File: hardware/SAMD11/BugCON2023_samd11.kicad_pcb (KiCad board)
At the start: 2 copper layers, 122.4 x 97.9 mm, 35 parts, among them J1 I2C, J3 PAD2, J4 PAD, P1 USB_C_Plug_USB2.0, Q1 DMG3415U-7, SW2 ON, U1 ATSAMD11C14A-SS, U2 AP2112K-3.3

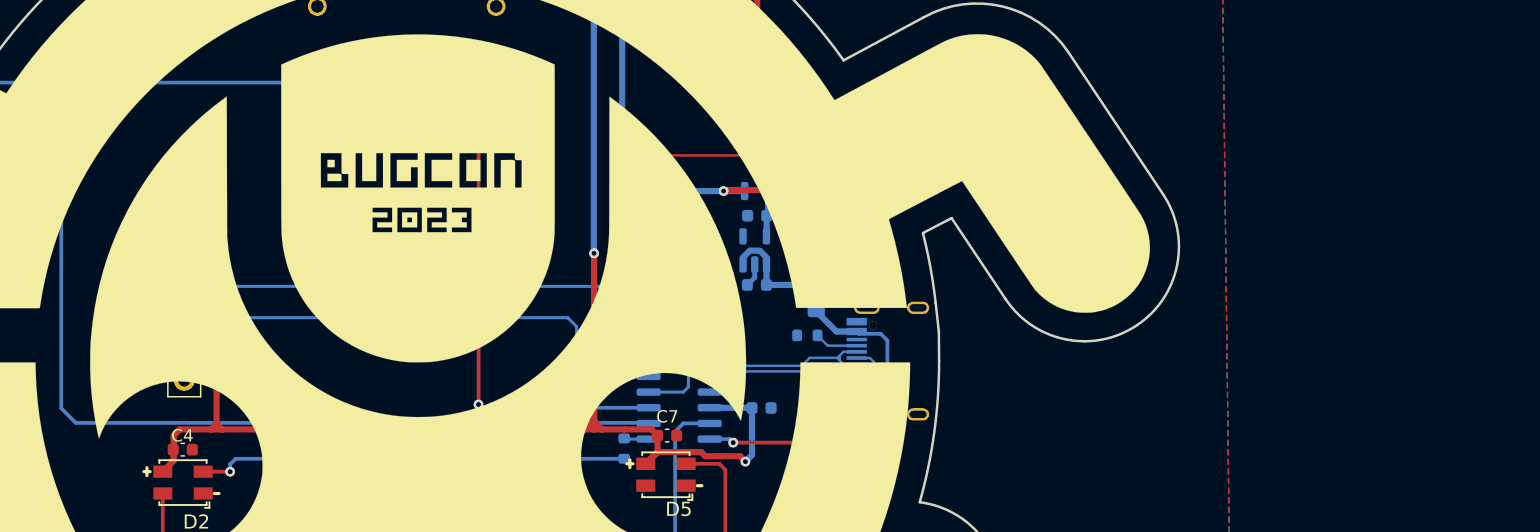
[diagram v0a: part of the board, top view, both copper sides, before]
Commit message: change MCU for RP2040
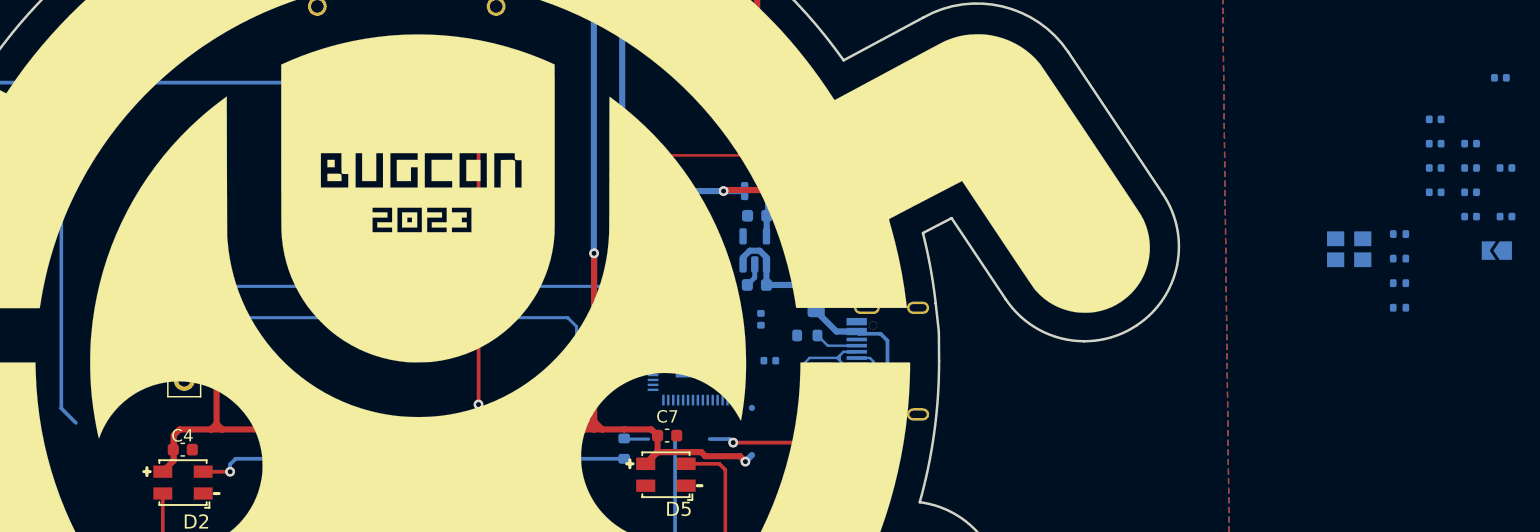
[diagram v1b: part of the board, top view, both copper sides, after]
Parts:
- removed U1: ATSAMD11C14A-SS, Package_SO:SOIC-14_3.9x8.7mm_P1.27mm
- added C10: 0.1uF, Capacitor_SMD:C_0402_1005Metric, B.Cu at (167.7, 101.7)
- added C11: 27pF, Capacitor_SMD:C_0402_1005Metric, B.Cu at (238.7, 90.3)
- added C12: 0.1uF, Capacitor_SMD:C_0402_1005Metric, B.Cu at (179.0, 102.0)
- added C13: 1uF, Capacitor_SMD:C_0402_1005Metric, B.Cu at (235.8, 84.4)
- added C14: 0.1uF, Capacitor_SMD:C_0402_1005Metric, B.Cu at (235.8, 86.4)
- added C15: 0.1uF, Capacitor_SMD:C_0402_1005Metric, B.Cu at (235.8, 88.3)
- added C16: 0.1uF, Capacitor_SMD:C_0402_1005Metric, B.Cu at (235.8, 90.3)
- added C17: 0.1uF, Capacitor_SMD:C_0402_1005Metric, B.Cu at (233.0, 82.4)
- added C18: 0.1uF, Capacitor_SMD:C_0402_1005Metric, B.Cu at (233.0, 84.4)
- added C19: 0.1uF, Capacitor_SMD:C_0402_1005Metric, B.Cu at (233.0, 86.4)
- added C20: 0.1uF, Capacitor_SMD:C_0402_1005Metric, B.Cu at (233.0, 88.3)
- added C8: 1uF, Capacitor_SMD:C_0402_1005Metric, B.Cu at (178.3, 98.7)
- added C9: 27pF, Capacitor_SMD:C_0402_1005Metric, B.Cu at (238.7, 86.4)
- added JP1: BOOT, Jumper:SolderJumper-2_P1.3mm_Open_TrianglePad1.0x1.5mm, B.Cu at (238.0, 93.1)
- added R10: 10k, Resistor_SMD:R_0402_1005Metric, B.Cu at (230.1, 97.7)
- added R7: 27, Resistor_SMD:R_0402_1005Metric, B.Cu at (230.1, 91.7)
- added R8: 27, Resistor_SMD:R_0402_1005Metric, B.Cu at (230.1, 93.7)
- added R9: 1k, Resistor_SMD:R_0402_1005Metric, B.Cu at (230.1, 95.7)
- added U3: RP2040, Package_DFN_QFN:QFN-56-1EP_7x7mm_P0.4mm_EP3.2x3.2mm, B.Cu at (173.0, 101.8)
- added Y1: 12MHz, Crystal:Crystal_SMD_3225-4Pin_3.2x2.5mm, B.Cu at (226.0, 93.0)
- C1: value 100nF -> 0.1uF; footprint Capacitor_SMD:C_0603_1608Metric -> Capacitor_SMD:C_0402_1005Metric
- moved C1 65.6 mm to (238.3, 79.1), turned to 180 degrees
- renumbered JE to J5
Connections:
- J4 pad : /IN1 -> (no net)
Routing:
- net /TX: track 94.6 -> 48.1 mm
- net /RX: track 95.4 -> 81.8 mm
- net /SDA: track 55.4 -> 44.5 mm
- net /D+: track 16.0 -> 8.16 mm
- net /D-: track 14.8 -> 7.20 mm
- net +3.3V: track 172.5 -> 165.2 mm
- net /RST: track 63.7 -> 57.3 mm
- net /SCL: track 44.3 -> 40.0 mm
- net /IN2: track 94.0 -> 90.9 mm
- net GND: vias 3 -> 2

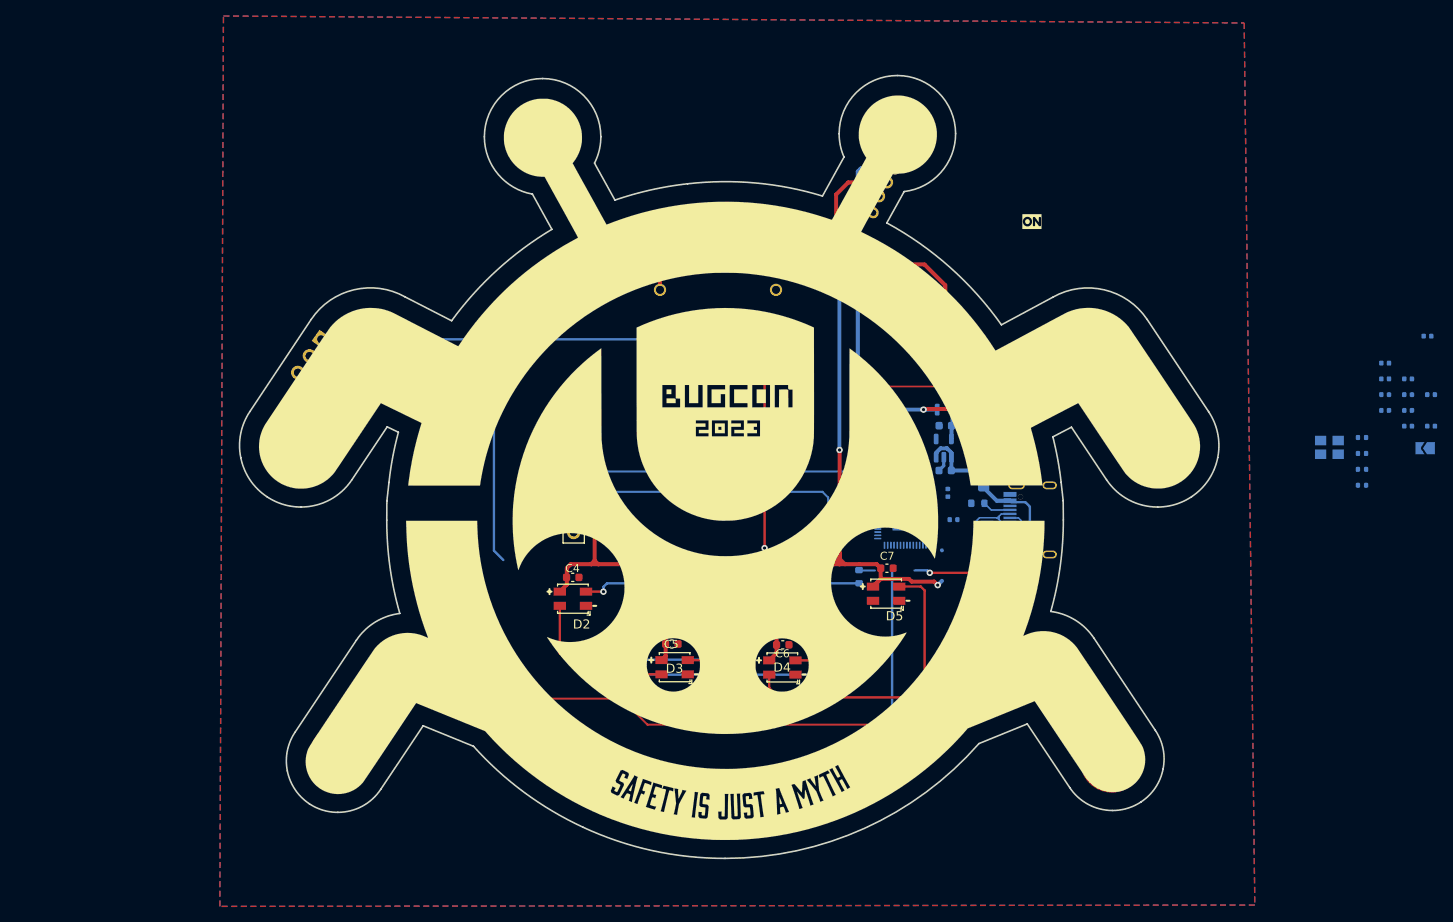
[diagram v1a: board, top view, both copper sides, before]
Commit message: upd floorplan on rp2040 badge
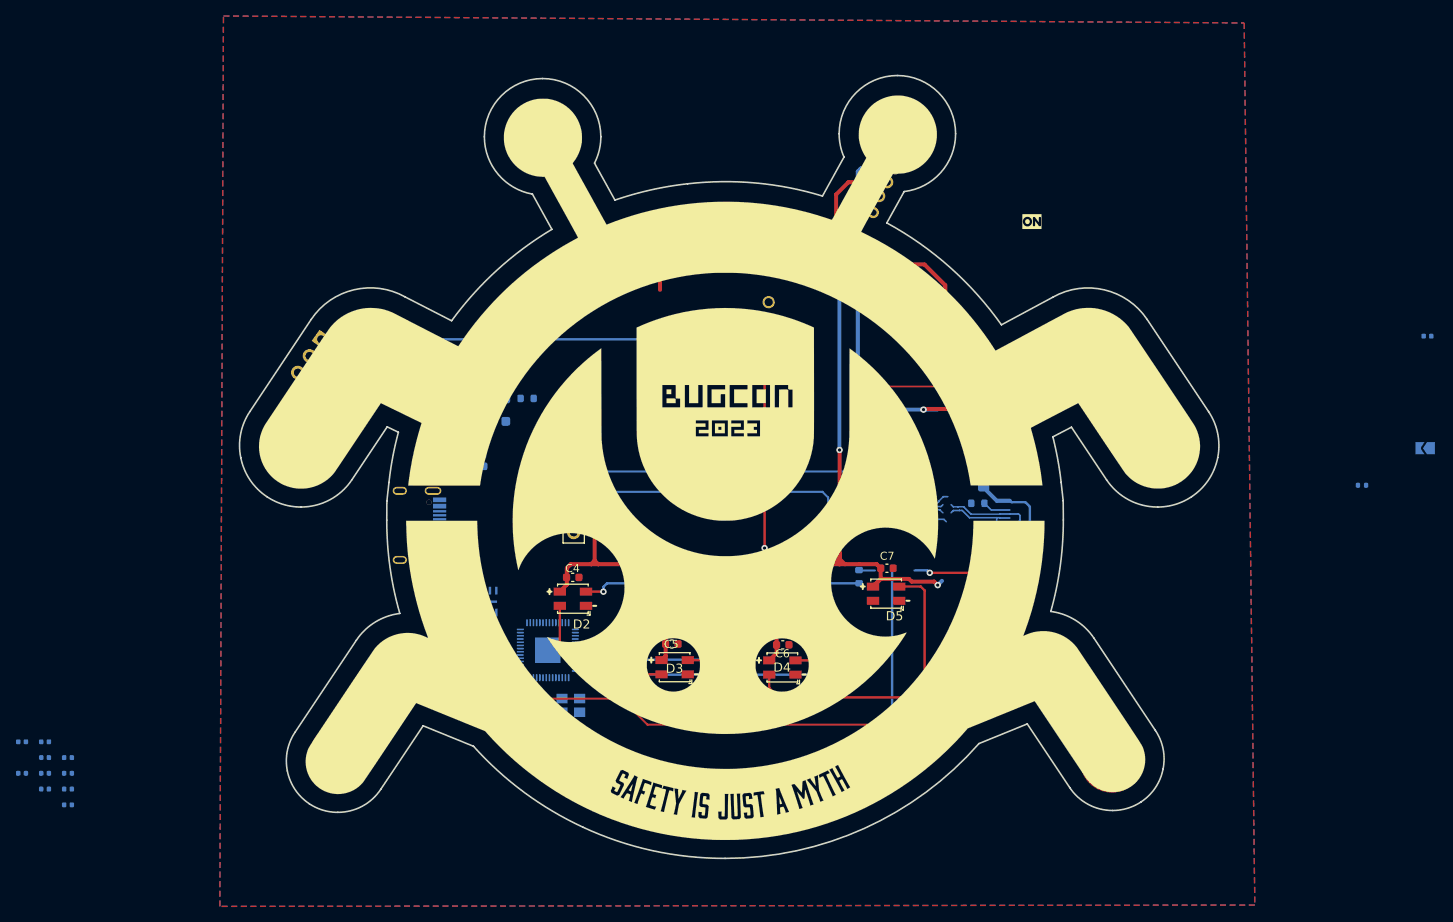
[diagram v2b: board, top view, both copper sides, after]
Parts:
- removed RST: SW_Push, Button_Switch_SMD:SW_SPST_TL3342
- added RESET1: SW, Button_Switch_SMD:SW_SPST_TL3342, B.Cu at (204.5, 93.1)
- added U1: W25Q16JV, BugCON2023_samd11:W25Q16JVUUIQ, B.Cu at (120.7, 112.2)
- moved C9 182.4 mm to (62.6, 133.7), turned to 0 degrees
- moved C11 180.5 mm to (62.6, 129.8), turned to 0 degrees
- moved C13 177.9 mm to (65.5, 135.7), turned to 0 degrees
- moved C14 176.8 mm to (65.5, 133.7), turned to 0 degrees
- moved C15 175.8 mm to (65.5, 131.7), turned to 0 degrees
- moved C16 174.9 mm to (65.5, 129.8), turned to 0 degrees
- moved C17 173.7 mm to (68.3, 137.7), turned to 0 degrees
- moved C18 172.4 mm to (68.3, 135.7), turned to 0 degrees
- moved C19 171.3 mm to (68.3, 133.7), turned to 0 degrees
- moved C20 170.3 mm to (68.3, 131.7), turned to 0 degrees
- moved R7 110.4 mm to (123.1, 118.9), turned to 0 degrees
- moved R8 110.2 mm to (123.1, 120.0), turned to 0 degrees
- moved Y1 100.2 mm to (131.2, 125.2), turned to 0 degrees
- moved R9 99.3 mm to (133.5, 119.1), turned to 90 degrees
- moved P1 72.9 mm to (114.0, 102.7), turned to 90 degrees
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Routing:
- net /RST: track 57.3 -> 0.00 mm, vias 2 -> 0
- net /RESET: track 0.00 -> 57.3 mm, vias 0 -> 2
- net /TX: track 48.1 -> 0.00 mm
- net +3V3: track 8.64 -> 0.00 mm
- net VBUS: track 9.28 -> 2.26 mm
- net /SDA: track 44.5 -> 38.1 mm
- net +1V2: track 0.00 -> 4.05 mm
- net /D-: track 7.20 -> 11.1 mm
- net /D+: track 8.16 -> 10.3 mm
- net Net-(U3-XOUT): track 0.00 -> 1.97 mm
- net GND: track 1.91 -> 0.00 mm
- net Net-(U3-USB_DP): track 0.00 -> 1.42 mm
- net Net-(U3-USB_DM): track 0.00 -> 1.37 mm

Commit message: Start new routing RP2040
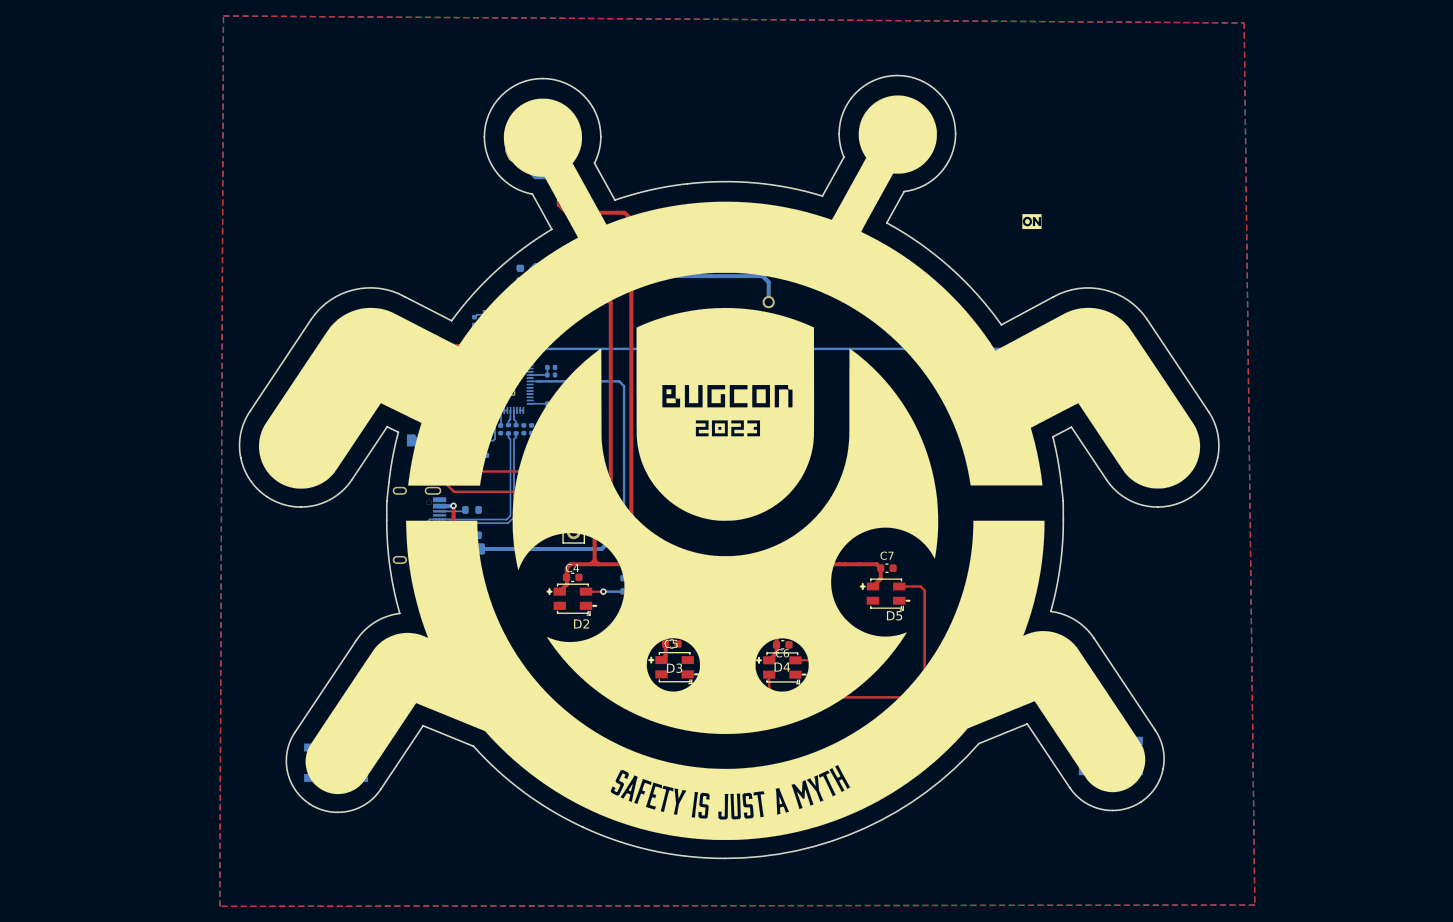
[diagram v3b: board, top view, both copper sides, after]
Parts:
- removed J3: PAD2, BugCON2023_samd11:Piad
- removed J4: PAD, BugCON2023_samd11:Piad
- added ?: , clipboard:c08f7a87-874b-4e71-adde-e6fa520882c1, F.Cu at (123.9, 86.2)
- added R11: 10K, Resistor_SMD:R_0603_1608Metric, B.Cu at (102.8, 126.8)
- added R12: 10K, Resistor_SMD:R_0603_1608Metric, B.Cu at (195.9, 125.6)
- added SW3: SW_Push, Button_Switch_SMD:SW_SPST_TL3342, B.Cu at (101.8, 132.4)
- added SW4: SW_Push, Button_Switch_SMD:SW_SPST_TL3342, B.Cu at (198.7, 131.6)
- SW1: renamed from RESET1; value SW -> RESET
- U1: footprint BugCON2023_samd11:W25Q16JVUUIQ -> BugCON2023_samd11:W25Q16JVUXIQ_WIN
- moved JP1 126.1 mm to (111.9, 92.1), turned to 0 degrees
- moved C1 119.0 mm to (120.2, 94.0), turned to 0 degrees
- moved R10 113.8 mm to (116.4, 93.9)
- moved C13 82.3 mm to (128.7, 83.0)
- moved C11 81.4 mm to (124.8, 77.2), turned to 90 degrees
- moved C9 80.0 mm to (119.1, 77.2), turned to -90 degrees
- moved C15 79.3 mm to (128.7, 83.9)
- moved C16 78.6 mm to (125.5, 79.1), turned to 90 degrees
- moved C17 78.5 mm to (128.7, 87.5)
- moved C19 75.5 mm to (128.7, 88.5)
- moved C18 73.4 mm to (126.3, 90.7), turned to -90 degrees
- moved C14 71.1 mm to (116.7, 84.4), turned to 180 degrees
- moved C20 65.5 mm to (116.7, 87.5), turned to 180 degrees
- moved F1 64.3 mm to (119.0, 105.7), turned to 0 degrees
- moved R2 64.3 mm to (118.8, 100.8), turned to 180 degrees
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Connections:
- net Net-(U3-USB_DM) renamed /RD-
- net Net-(U3-USB_DP) renamed /RD+
- JP1 pad 2: /QSPI_CS -> /QSPI_SS
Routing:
- net /IN2: track 90.9 -> 0.00 mm, vias 1 -> 0
- net VBUS: track 2.26 -> 67.1 mm, vias 0 -> 2
- net /RX: track 81.8 -> 19.5 mm, vias 2 -> 0
- net /RESET: track 57.3 -> 96.7 mm, vias 2 -> 0
- net /IN1: track 36.0 -> 0.00 mm, vias 1 -> 0
- net /PIN: track 2.01 -> 36.5 mm
- net Net-(D1-K): track 55.3 -> 22.8 mm, vias 2 -> 0
- net +BATT: track 53.1 -> 22.0 mm, vias 1 -> 0
- net Net-(D2-DIN): track 34.9 -> 4.38 mm
- net Net-(D2-DOUT): track 26.9 -> 0.00 mm, vias 2 -> 0
- net Net-(D3-DOUT): track 26.7 -> 3.89 mm, vias 2 -> 1
- net /TX: track 0.00 -> 22.4 mm
- net +3.3V: track 165.2 -> 178.9 mm, vias 3 -> 0
- net /D-: track 11.1 -> 24.1 mm
- net /D+: track 10.3 -> 23.1 mm
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
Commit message: Update routing RP2040
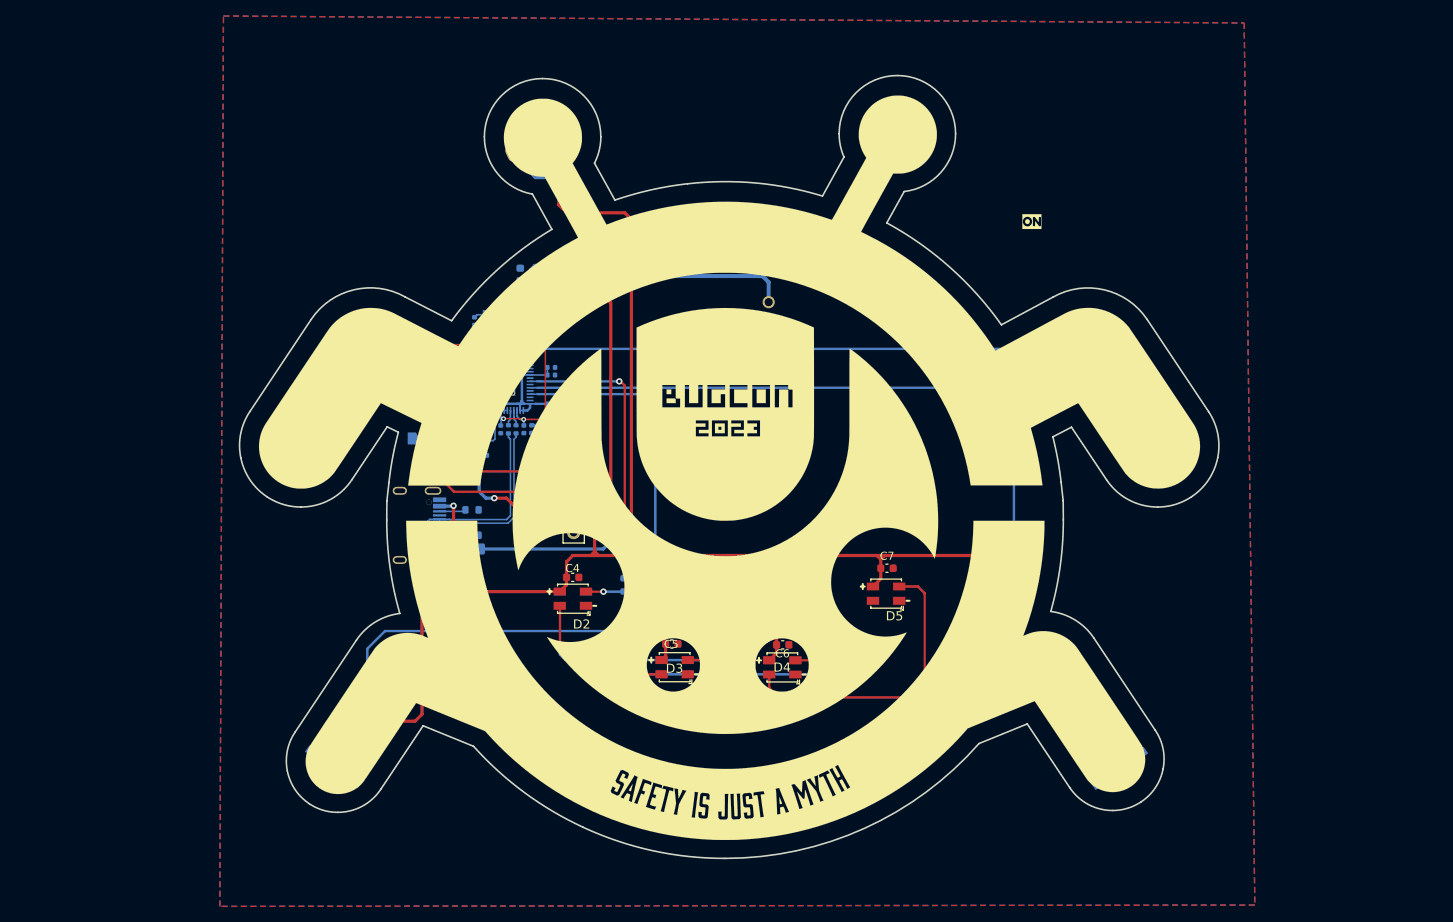
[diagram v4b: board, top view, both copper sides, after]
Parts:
- moved R11 4.02 mm to (106.4, 128.4), turned to 145 degrees
- moved R12 3.17 mm to (195.1, 128.6), turned to 35 degrees
- moved SW3 1.30 mm to (102.6, 131.3), turned to 145 degrees
- moved JP1 0.28 mm to (112.0, 91.8)
- turned SW4 to -145 degrees
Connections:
- U3 pad 37: unconnected-(U3-GPIO25-Pad37) -> /PB2
- U3 pad 39: unconnected-(U3-GPIO27_ADC1-Pad39) -> /PB1
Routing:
- net +3.3V: track 178.9 -> 338.6 mm, vias 0 -> 4
- net /PB2: track 0.00 -> 121.4 mm
- net /PB1: track 0.00 -> 101.0 mm
- net Net-(D2-DOUT): track 0.00 -> 27.0 mm, vias 0 -> 2
- net Net-(D3-DOUT): track 3.89 -> 30.7 mm, vias 1 -> 2
- net +1V2: track 6.53 -> 26.4 mm, vias 0 -> 3
- net GND: track 0.00 -> 3.44 mm
- net /QSPI_SS: track 12.1 -> 15.5 mm
- net /PIN: track 36.5 -> 36.7 mm, vias 0 -> 2
